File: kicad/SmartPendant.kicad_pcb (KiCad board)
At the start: 2 copper layers, 125 x 59 mm, 51 parts, among them J1 UART, J2 ST-LINK, J3 Encoder, J5 Display, J6 USB_C_Receptacle_USB2.0_16P, J8 Micro_SD_Card_Det1, Q1 MMBT3904, U1 WEACT BLACKPILL F4X1, U2 AMS1117-3.3, U3 MB85RC256VPNF-G-JNERE1

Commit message: Start routing.
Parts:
- moved D3 31.7 mm to (174.0, 104.3), turned to 0 degrees
- moved C2 24.7 mm to (155.1, 101.9)
- moved C5 14.9 mm to (231.1, 72.9)
- moved R1 14.6 mm to (187.9, 99.3), turned to 180 degrees
- moved Q1 14.3 mm to (188.4, 102.4)
- moved C8 10.1 mm to (160.4, 60.7)
- moved C1 9.53 mm to (169.1, 100.0), turned to -90 degrees
- moved C10 7.13 mm to (169.8, 65.8)
- moved BZ1 6.32 mm to (181.1, 97.4)
- moved R6 5.56 mm to (157.2, 99.4), turned to 0 degrees
- moved C6 3.23 mm to (243.2, 84.3)
- moved R17 1.72 mm to (239.2, 65.8)
- moved R23 1.72 mm to (232.0, 65.8), turned to 90 degrees
- moved R24 1.72 mm to (237.2, 65.8)
- moved R22 1.72 mm to (230.2, 65.8)
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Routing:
- net GND: track 0.00 -> 103.7 mm
- net SWDIO: track 0.00 -> 85.2 mm, vias 0 -> 2
- net SWCLK: track 0.00 -> 76.3 mm, vias 0 -> 2
- net SDIO_D0: track 0.00 -> 66.5 mm, vias 0 -> 1
- net LCD_DC: track 0.00 -> 65.9 mm, vias 0 -> 1
- net SDIO_CMD: track 0.00 -> 63.3 mm, vias 0 -> 1
- net MPG_EN: track 0.00 -> 63.2 mm, vias 0 -> 1
- net SCL: track 0.00 -> 60.6 mm, vias 0 -> 1
- net LCD_CS: track 0.00 -> 58.5 mm, vias 0 -> 1
- net SDA: track 0.00 -> 55.9 mm, vias 0 -> 2
- net USB_DP: track 0.00 -> 53.0 mm
- net Net-(J2-Pin_1): track 0.00 -> 50.7 mm
- net USB_DN: track 0.00 -> 50.4 mm
- net LCD_RST: track 0.00 -> 50.2 mm, vias 0 -> 1
- net TOUCH_RST: track 0.00 -> 46.3 mm, vias 0 -> 1
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
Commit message: Route some more.
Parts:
- moved C3 39.7 mm to (241.8, 61.4), turned to -90 degrees
- moved C7 7.70 mm to (210.9, 60.9), turned to 90 degrees
- moved R10 2.42 mm to (214.3, 99.8)
- turned R13 to 180 degrees
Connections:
- BTN_USR1 pad 1: USR_BTN -> GND
- BTN_USR1 pad 2: GND -> USR_BTN
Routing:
- net GND: track 103.7 -> 253.7 mm, vias 0 -> 5
- net ENC_B: track 0.00 -> 63.8 mm, vias 0 -> 3
- net ENC_A: track 0.00 -> 59.6 mm, vias 0 -> 2
- net BTN_RD: track 0.00 -> 46.9 mm, vias 0 -> 1
- net BTN_LU: track 0.00 -> 36.9 mm, vias 0 -> 1
- net BTN_LD: track 0.00 -> 35.0 mm, vias 0 -> 1
- net BTN_RU: track 0.00 -> 33.4 mm, vias 0 -> 1
- net BAT: track 0.00 -> 31.8 mm, vias 0 -> 2
- net +3.3V: track 18.1 -> 45.3 mm, vias 0 -> 2
- net VCC: track 28.7 -> 54.8 mm, vias 0 -> 2
- net RIGHT_BTN: track 44.1 -> 57.8 mm, vias 0 -> 1
- net LEFT_BTN: track 0.00 -> 3.39 mm, vias 0 -> 1
- net USR_BTN: track 0.00 -> 3.01 mm
- net LCD_MISO: track 41.9 -> 43.3 mm
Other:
- board text added: "SmartPendant"

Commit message: More routing.
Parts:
- moved C5 70.1 mm to (161.2, 67.7), turned to 90 degrees
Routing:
- net VCC: track 54.8 -> 236.5 mm, vias 2 -> 11
- net +5V: track 17.2 -> 137.0 mm, vias 0 -> 6
- net GND: track 253.7 -> 351.0 mm, vias 5 -> 8
- net USR_BTN: track 3.01 -> 76.2 mm, vias 0 -> 1
- net LEFT_BTN: track 3.39 -> 62.2 mm, vias 1 -> 2
- net SDIO_CD: track 2.40 -> 44.5 mm, vias 0 -> 3
- net +3.3V: track 45.3 -> 85.2 mm, vias 2 -> 4
- net USB_DN: track 50.4 -> 53.6 mm
- net BTN_LU: track 36.9 -> 39.9 mm
- net SCL: track 60.6 -> 62.9 mm
- net RIGHT_BTN: track 57.8 -> 55.7 mm, vias 1 -> 3
- net TOUCH_RST: track 46.3 -> 45.0 mm

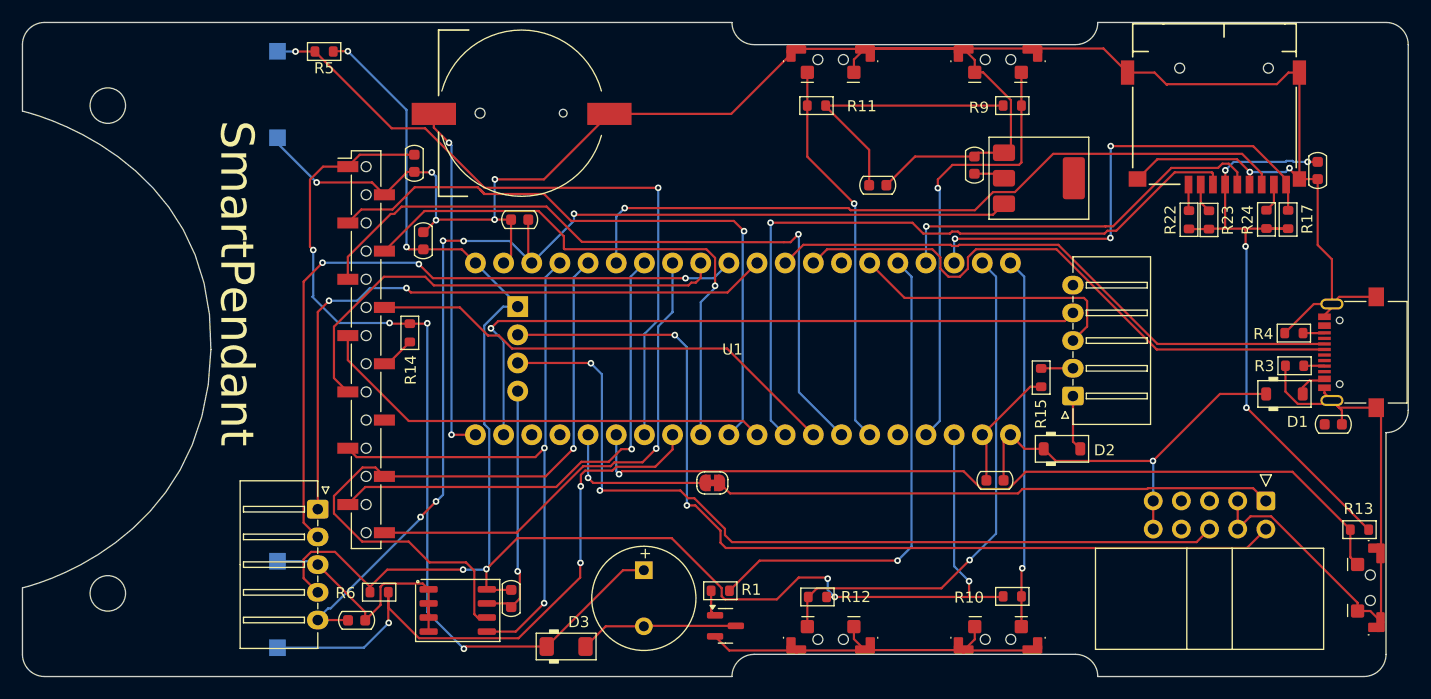
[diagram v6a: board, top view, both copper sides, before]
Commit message: Complete routing.
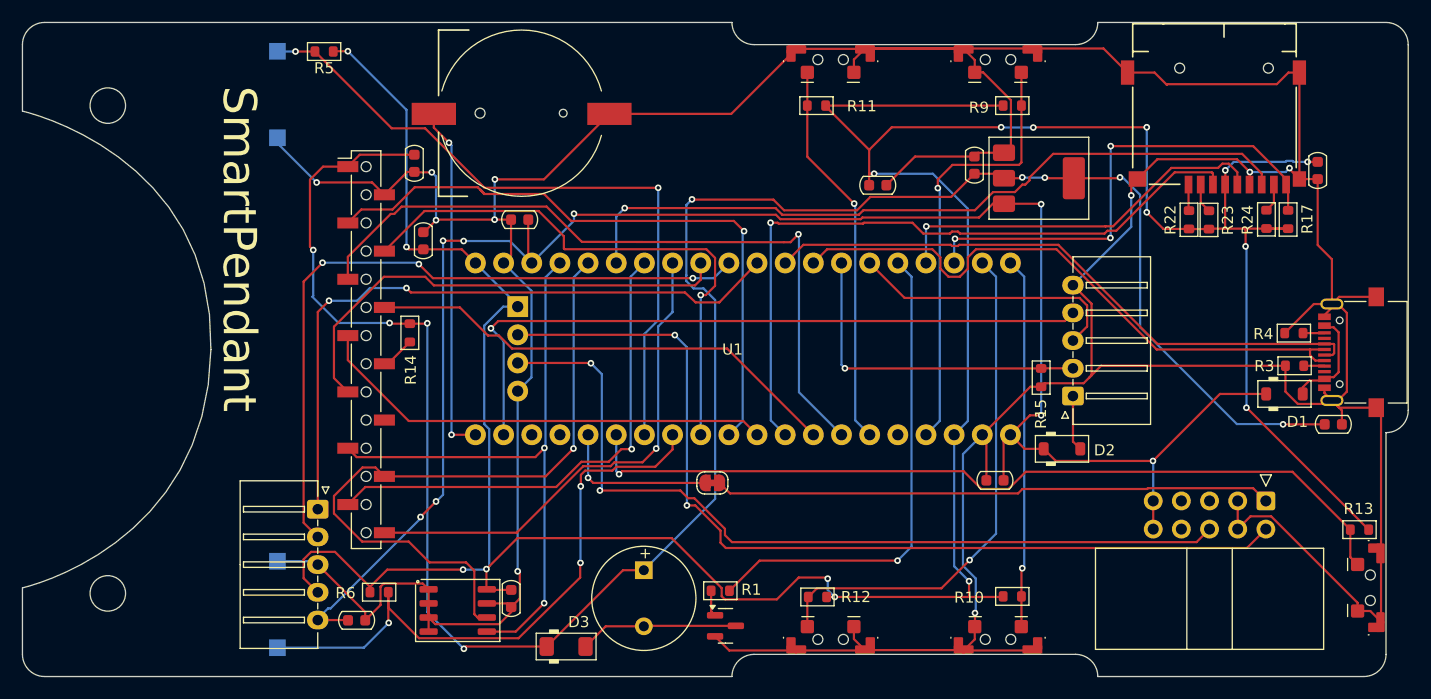
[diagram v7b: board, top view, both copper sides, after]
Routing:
- net +3.3V: track 85.2 -> 195.6 mm, vias 4 -> 9
- net GND: track 351.0 -> 445.6 mm, vias 8 -> 10
- net VCC: track 236.5 -> 305.6 mm, vias 11 -> 16
- net UART_RX: track 2.88 -> 30.2 mm, vias 0 -> 1
- net +5V: track 137.0 -> 163.2 mm, vias 6 -> 8
- net Net-(D1-A): track 2.81 -> 9.34 mm
- net USB_DP: track 53.1 -> 55.7 mm
- net USB_DN: track 53.6 -> 55.6 mm
- net ENC_A: track 59.6 -> 60.3 mm

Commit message: Add ground planes.
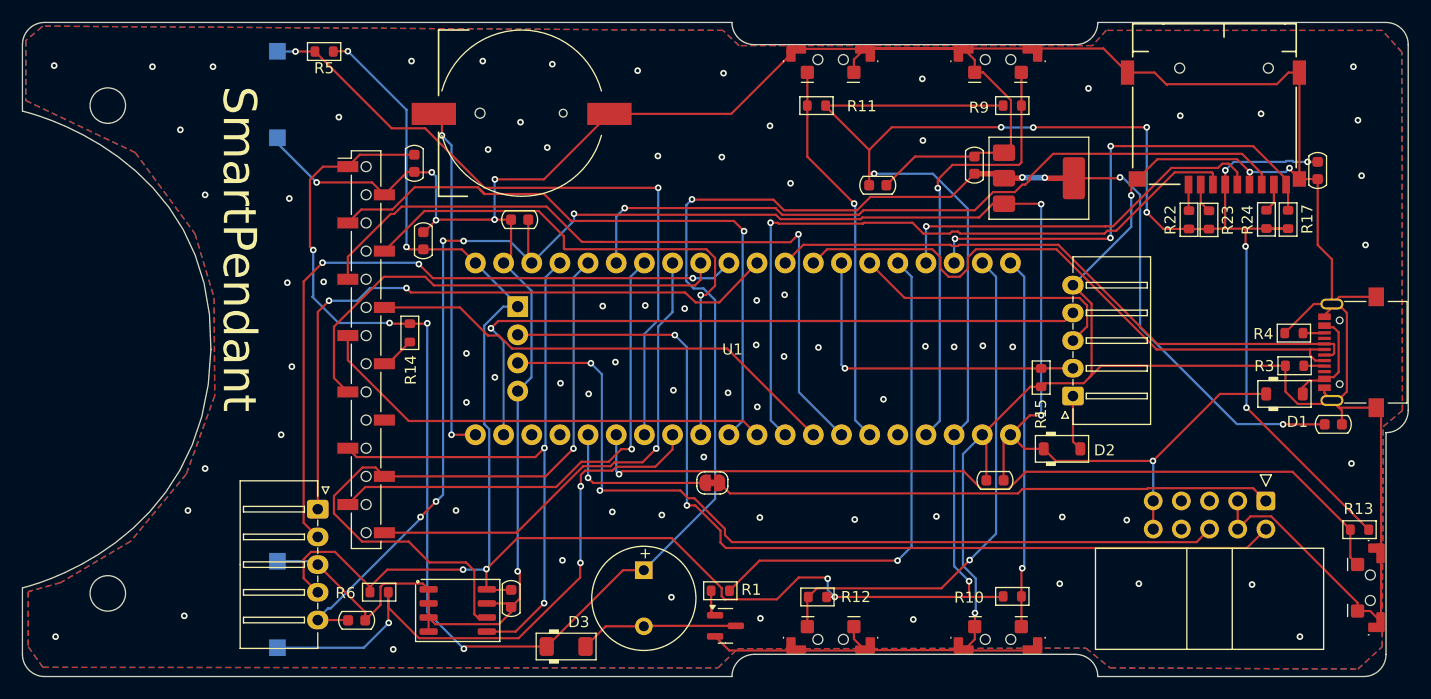
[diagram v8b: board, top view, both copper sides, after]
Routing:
- net GND: vias 10 -> 87
- added copper zone on B.Cu, net GND
- added copper zone on F.Cu, net GND
